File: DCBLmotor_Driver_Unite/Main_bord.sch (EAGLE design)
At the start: 72 parts, among them CN1 DF11-16DP-2DSA, CN2 DF11-16DP-2DSA, CN3 DF11-4DP-2DSR, CN4 HIF3FC-10PA-2.54DSA(71), CN5 HIF3FC-10PA-2.54DSA(71), CN6 0430450612, CN7 0430450612, CN8 BM11B-SRSS-TB, IC1 TMPM370FYFG, IC2 MCP2561FD-E/MF, IC3 AM26C32CD, IC4 AM26C32CD, IC5 LTC2862A, SW1 CVS-02TB, SW2 EVQ-PE104K

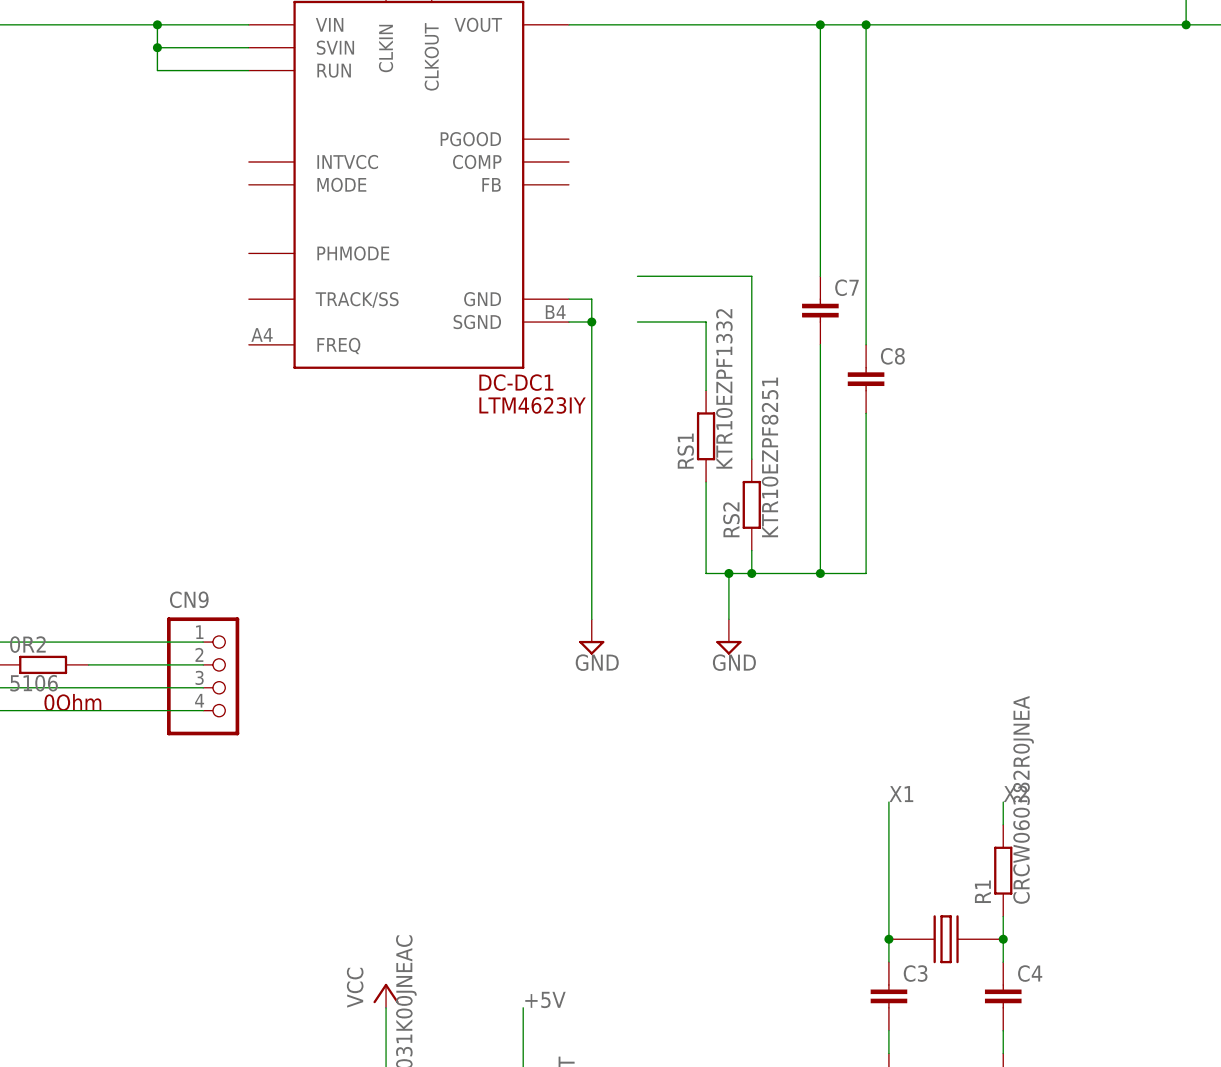
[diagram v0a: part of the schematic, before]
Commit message: Repless to LTM4623
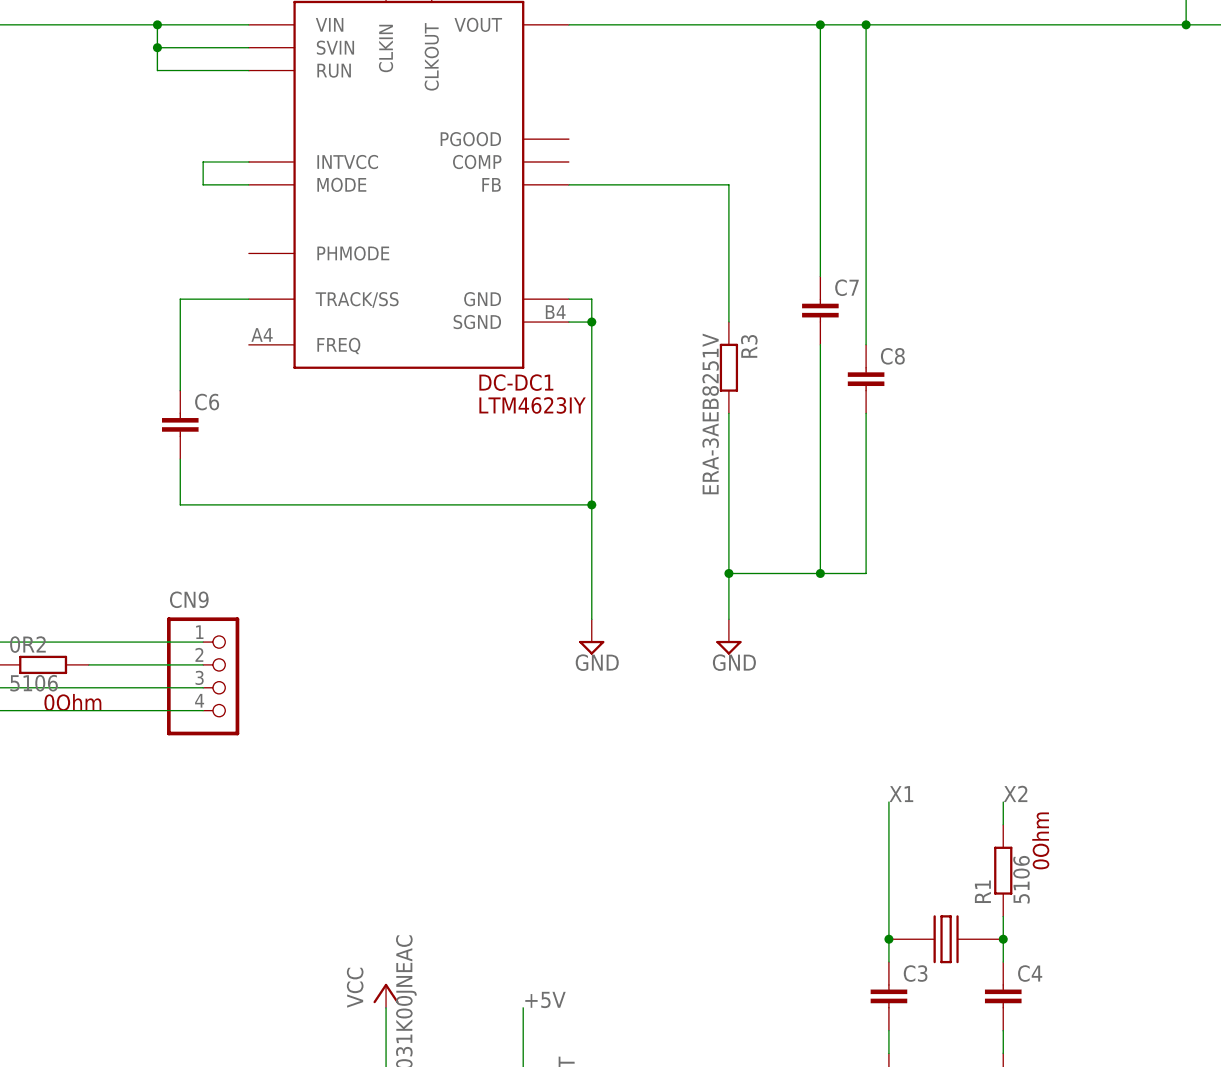
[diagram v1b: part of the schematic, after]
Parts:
- removed RS1: KTR10EZPF1332, ROHM:KTR10EZPF1332
- removed RS2: KTR10EZPF8251, ROHM:KTR10EZPF8251
- added C6: CGA3E2X7R1H104K080AA, TDK:CGA3E2X7R1H104K080AA
- added R3: ERA-3AEB8251V, Panasonic:ERA-3AEB8251V
- R1: value CRCW060382R0JNEA -> 5106; device VISHAY:CRCW060382R0JNEA -> Keystone:5106
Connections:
- removed net N$10: RS2.1
- new net N$12: C6.1, DC-DC1.TRACK/SS
- new net N$45: DC-DC1.INTVCC, DC-DC1.MODE
- net GND: now also C6.2, R3.1; no longer RS1.2, RS2.2
- net N$7: now also DC-DC1.FB, R3.2; no longer RS1.1
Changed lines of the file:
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@@
 <part name="SUPPLY3" library="supply2" library_urn="urn:adsk.eagle:library:372" deviceset="GND" device=""/>
 <part name="SUPPLY5" library="supply2" library_urn="urn:adsk.eagle:library:372" deviceset="GND" device=""/>
-<part name="RS1" library="ROHM" deviceset="KTR10EZPF1332" device=""/>
-<part name="RS2" library="ROHM" deviceset="KTR10EZPF8251" device=""/>
 <part name="SUPPLY8" library="supply2" library_urn="urn:adsk.eagle:library:372" deviceset="GND" device=""/>
 <part name="C7" library="TDK" deviceset="C2012JB0J476M125AC" device=""/>
@@
 <part name="CN1" library="Hirose" deviceset="DF11-16DP-2DSA" device=""/>
 <part name="CN2" library="Hirose" deviceset="DF11-16DP-2DSA" device=""/>
-<part name="R1" library="VISHAY" deviceset="CRCW060382R0JNEA" device=""/>
+<part name="R1" library="Keystone" deviceset="5106" device=""/>
 <part name="L1" library="LQW21HN1R0J00L" deviceset="LQW21HN1R0J00L" device=""/>
 <part name="SUPPLY13" library="supply2" library_urn="urn:adsk.eagle:library:372" deviceset="GND" device=""/>
@@
 <part name="C5" library="KEMET" deviceset="T356L107K016AT" device=""/>
 <part name="DC-DC1" library="LT" deviceset="LTM4623IY" device=""/>
+<part name="C6" library="TDK" deviceset="CGA3E2X7R1H104K080AA" device=""/>
+<part name="R3" library="Panasonic" deviceset="ERA-3AEB8251V" device=""/>
 </parts>
 <sheets>
@@
 <instance part="SUPPLY3" gate="GND" x="416.56" y="-17.78"/>
 <instance part="SUPPLY5" gate="GND" x="78.74" y="-127"/>
-<instance part="RS1" gate="G$1" x="429.26" y="5.08" rot="R90"/>
-<instance part="RS2" gate="G$1" x="434.34" y="-2.54" rot="R90"/>
 <instance part="SUPPLY8" gate="GND" x="431.8" y="-17.78"/>
 <instance part="C7" gate="G$1" x="441.96" y="20.32"/>
@@
 <instance part="C5" gate="G$1" x="439.42" y="220.98"/>
 <instance part="DC-DC1" gate="G$1" x="396.24" y="33.02"/>
+<instance part="C6" gate="G$1" x="370.84" y="7.62"/>
+<instance part="R3" gate="G$1" x="431.8" y="12.7" rot="R270"/>
 </instances>
 <busses>
@@
 <net name="GND" class="0">
 <segment>
-<pinref part="RS1" gate="G$1" pin="2"/>
-<wire x1="429.26" y1="0" x2="429.26" y2="-10.16" width="0.1524" layer="91"/>
-<pinref part="RS2" gate="G$1" pin="2"/>
-<wire x1="434.34" y1="-7.62" x2="434.34" y2="-10.16" width="0.1524" layer="91"/>
-<wire x1="434.34" y1="-10.16" x2="431.8" y2="-10.16" width="0.1524" layer="91"/>
 <pinref part="SUPPLY8" gate="GND" pin="GND"/>
-<wire x1="431.8" y1="-10.16" x2="429.26" y2="-10.16" width="0.1524" layer="91"/>
 <wire x1="431.8" y1="-10.16" x2="431.8" y2="-15.24" width="0.1524" layer="91"/>
-<junction x="431.8" y="-10.16"/>
 <pinref part="C8" gate="G$1" pin="2"/>
-<wire x1="434.34" y1="-10.16" x2="441.96" y2="-10.16" width="0.1524" layer="91"/>
+<wire x1="431.8" y1="-10.16" x2="441.96" y2="-10.16" width="0.1524" layer="91"/>
 <wire x1="441.96" y1="-10.16" x2="447.04" y2="-10.16" width="0.1524" layer="91"/>
 <wire x1="447.04" y1="-10.16" x2="447.04" y2="7.62" width="0.1524" layer="91"/>
-<junction x="434.34" y="-10.16"/>
 <pinref part="C7" gate="G$1" pin="2"/>
 <wire x1="441.96" y1="15.24" x2="441.96" y2="-10.16" width="0.1524" layer="91"/>
 <junction x="441.96" y="-10.16"/>
+<pinref part="R3" gate="G$1" pin="1"/>
+<wire x1="431.8" y1="7.62" x2="431.8" y2="-10.16" width="0.1524" layer="91"/>
+<junction x="431.8" y="-10.16"/>
 </segment>
 <segment>
@@
 <junction x="416.56" y="17.78"/>
 <pinref part="SUPPLY3" gate="GND" pin="GND"/>
-<wire x1="416.56" y1="-15.24" x2="416.56" y2="17.78" width="0.1524" layer="91"/>
-</segment>
-</net>
-<net name="N$7" class="0">
-<segment>
-<pinref part="RS1" gate="G$1" pin="1"/>
-<wire x1="421.64" y1="17.78" x2="429.26" y2="17.78" width="0.1524" layer="91"/>
-<wire x1="429.26" y1="17.78" x2="429.26" y2="10.16" width="0.1524" layer="91"/>
-</segment>
-</net>
-<net name="N$10" class="0">
-<segment>
-<pinref part="RS2" gate="G$1" pin="1"/>
-<wire x1="421.64" y1="22.86" x2="434.34" y2="22.86" width="0.1524" layer="91"/>
-<wire x1="434.34" y1="22.86" x2="434.34" y2="2.54" width="0.1524" layer="91"/>
+<wire x1="416.56" y1="-15.24" x2="416.56" y2="-2.54" width="0.1524" layer="91"/>
+<pinref part="C6" gate="G$1" pin="2"/>
+<wire x1="416.56" y1="-2.54" x2="416.56" y2="17.78" width="0.1524" layer="91"/>
+<wire x1="370.84" y1="2.54" x2="370.84" y2="-2.54" width="0.1524" layer="91"/>
+<wire x1="370.84" y1="-2.54" x2="416.56" y2="-2.54" width="0.1524" layer="91"/>
+<junction x="416.56" y="-2.54"/>
 </segment>
 </net>
@@
 </segment>
 </net>
+<net name="N$12" class="0">
+<segment>
+<pinref part="C6" gate="G$1" pin="1"/>
+<pinref part="DC-DC1" gate="G$1" pin="TRACK/SS"/>
+<wire x1="370.84" y1="10.16" x2="370.84" y2="20.32" width="0.1524" layer="91"/>
+<wire x1="370.84" y1="20.32" x2="378.46" y2="20.32" width="0.1524" layer="91"/>
+</segment>
+</net>
+<net name="N$45" class="0">
+<segment>
+<pinref part="DC-DC1" gate="G$1" pin="INTVCC"/>
+<wire x1="378.46" y1="35.56" x2="373.38" y2="35.56" width="0.1524" layer="91"/>
+<wire x1="373.38" y1="35.56" x2="373.38" y2="33.02" width="0.1524" layer="91"/>
+<pinref part="DC-DC1" gate="G$1" pin="MODE"/>
+<wire x1="373.38" y1="33.02" x2="378.46" y2="33.02" width="0.1524" layer="91"/>
+</segment>
+</net>
+<net name="N$7" class="0">
+<segment>
+<pinref part="DC-DC1" gate="G$1" pin="FB"/>
+<pinref part="R3" gate="G$1" pin="2"/>
+<wire x1="414.02" y1="33.02" x2="431.8" y2="33.02" width="0.1524" layer="91"/>
+<wire x1="431.8" y1="33.02" x2="431.8" y2="17.78" width="0.1524" layer="91"/>
+</segment>
+</net>

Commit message: TEMP Chenge MCU
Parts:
- removed C7, C8: C2012JB0J476M125AC, TDK:C2012JB0J476M125AC
- removed CN10: (no value), jst-xh:B2B-XH-A
- removed CN2: DF11-16DP-2DSA, Hirose:DF11-16DP-2DSA
- removed CN3: DF11-4DP-2DSR, Hirose:DF11-4DP-2DSR
- removed CN4, CN5: HIF3FC-10PA-2.54DSA(71), Hirose:HIF3FC-10PA-2.54DSA(71)
- removed CN6, CN7: 0430450612, Molex:0430450612
- removed CR10, CR11, CR8: NSI50010YT1G, ON Semiconductor:NSI50010YT1G
- removed DC-DC1: LTM4623IY, LT:LTM4623IY
- removed DC10, DC11, DC12, DC13, DC14: YFF21PC1E104MT000N, TDK:YFF21PC1E104MT000N
- removed IC3, IC4: AM26C32CD, AM26C32CD:AM26C32CD
- removed LED2: CL-340T-SD-T, Citizen:CL-340T-SD-T
- removed R1: 5106, Keystone:5106
- removed R3: ERA-3AEB8251V, Panasonic:ERA-3AEB8251V
- removed R4, R5: CRCW060360R4FKEA, VISHAY:CRCW060360R4FKEA
- removed VR1: 3314J-1-104E, Bourns:3314J-1-104E
- C3, C4: value CGA1A2C0G1E180J030BA -> GRM0225C1E120JA03L; device TDK:CGA1A2C0G1E180J030BA -> murata:GRM0225C1E120JA03L
- C5: value T356L107K016AT -> GRM035R60J475ME15D; device KEMET:T356L107K016AT -> murata:GRM035R60J475ME15D
- C6: value CGA3E2X7R1H104K080AA -> GRM035R60J475ME15D; device TDK:CGA3E2X7R1H104K080AA -> murata:GRM035R60J475ME15D
- CN1: value DF11-16DP-2DSA -> FX23L-20S-0.5SV; device Hirose:DF11-16DP-2DSA -> FX23L-20S-0.5SV:FX23L-20S-0.5SV
- DC9: value YFF21PC1E104MT000N -> YFF15PC1C104MT000N; device TDK:YFF21PC1E104MT000N -> TDK:YFF15PC1C104MT000N
- IC2: value MCP2561FD-E/MF -> TMPM373FWDUG; device MicroChip:MCP2561FD-E/MF -> TMPM373FWDUG:TMPM373FWDUG
- XTAL1: value HCM4910000000ABJT -> ABM8AIG-10.000MHZ-12-2Z-T3; device Citizen:HCM4910000000ABJT -> Abracon:ABM8AIG-10.000MHZ-12-2Z-T3
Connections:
- removed net 1SD: CN1.2
- removed net 1_A1: CN4.5, IC3.1B
- removed net 1_A2: CN4.6, IC3.1A
- removed net 1_B1: CN4.7, IC3.2A
- removed net 1_B2: CN4.8, IC3.2B
- removed net 1_I1: CN4.9, IC3.3A
- removed net 1_I2: CN4.10, IC3.3B
- removed net 2SD: CN2.2
- removed net 2_A1: CN5.5, IC4.1B
- removed net 2_A2: CN5.6, IC4.1A
- removed net 2_B1: CN5.7, IC4.2A
- removed net 2_B2: CN5.8, IC4.2B
- removed net CANH: CN3.1, IC2.CANH, R4.1
- removed net CANL: CN3.3, IC2.CANL, R5.1
- removed net N$12: C6.1, DC-DC1.TRACK/SS
- removed net N$28: DC10.P$2, IC4.VCC
- removed net N$29: DC9.P$2, IC3.VCC
- removed net N$30: CN5.2, DC12.P$2
- removed net N$31: CN4.2, DC11.P$2
- removed net N$32: CN6.P$5, DC13.P$2
- removed net N$33: CN7.P$5, DC14.P$2
- removed net N$35: CN5.9, IC4.3A
- removed net N$36: CN5.10, IC4.3B
- removed net N$40: CR8.P$A, LED2.B_C
- removed net N$41: CR11.P$A, LED2.R_C
- removed net N$42: CR10.P$A, LED2.G_C
- removed net N$45: DC-DC1.INTVCC, DC-DC1.MODE
- removed net SPLT: CN3.2, IC2.SPLT, R4.2, R5.2
- removed net VDD: C5.+, CN10.1, DC-DC1.RUN, DC-DC1.SVIN, DC-DC1.VIN
- new net N$10: DC8.P$1, IC2.DVDD5(2)
- net +5V: no longer C7.1, C8.1, DC-DC1.VOUT, DC10.P$1, DC11.P$1, DC12.P$1, DC13.P$1, DC14.P$1, DC8.P$2, DC9.P$1, LED2.A_G, LED2.B_A, LED2.R_A
- net 1U_H: no longer CN1.7
- net 1U_L: no longer CN1.8
- net 1V_H: no longer CN1.3
- net 1V_L: no longer CN1.4
- net 1W_H: no longer CN1.5
- net 1W_L: no longer CN1.6
- net 2U_H: no longer CN2.7
- net 2U_L: no longer CN2.8
- net 2V_H: no longer CN2.3
- net 2V_L: no longer CN2.4
- net 2W_H: no longer CN2.5
- net 2W_L: no longer CN2.6
- net AVDD: no longer VR1.1
- net CU1_1: no longer CN1.15
- net CU1_2: no longer CN1.14
- net CU1_3: no longer CN1.13
- net CU2_1: no longer CN2.15
- net CU2_2: no longer CN2.14
- net CU2_3: no longer CN2.13
- net CVR2: no longer VR1.IO3
- net ENC_A-1: no longer CN6.P$1, IC3.1Y
- net ENC_A-2: no longer CN7.P$1, IC4.1Y
- net ENC_B-1: no longer CN6.P$2, IC3.2Y
- net ENC_B-2: no longer CN7.P$2, IC4.2Y
- net ENC_Z-1: no longer CN6.P$3, IC3.3Y
- net ENC_Z-2: no longer CN7.P$3, IC4.3Y
- net GND: no longer C5.2, C6.2, C7.2, C8.2, CN10.2, CN4.3, CN5.3, CN6.P$4, CN7.P$4, DC-DC1.GND, DC-DC1.SGND, DC10.GND, DC11.GND, DC12.GND, DC13.GND, DC14.GND, DC8.GND, DC9.GND, IC2.VSS, IC3.GND, IC4.GND, R3.1, VR1.2
- net LED2_1: no longer CR10.P$C
- net LED2_2: no longer CR11.P$C
- net LED2_3: no longer CR8.P$C
- net N$11: now also DC9.P$2, IC2.DVDD5(1); no longer C4.1, R1.2, XTAL1.P$2
- net N$6: now also C5.1, IC2.VOUT15; no longer DC8.P$1, IC2.VDD
- net N$7: now also C6.1, IC2.VOUT3; no longer DC-DC1.FB, R3.2
- net RX0: no longer IC2.RXD
- net STBY: no longer IC2.STBY
- net TX0: no longer IC2.TXD
- net X1: now also C4.1, IC2.PM0/X1; no longer C3.1
- net X2: now also C3.1, IC2.PM1/X2, XTAL1.P$2; no longer R1.1
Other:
- moved on the sheet: C3, C4, C6, DC8, DC9

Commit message: Main_borad is Almost_finshed
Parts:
- removed 0R1, 0R2: 5106, Keystone:5106
- removed C1, C2: C2012X7R1A475M125AC, TDK:C2012X7R1A475M125AC
- removed CN8: BM11B-SRSS-TB, JST:BM11B-SRSS-TB
- removed CR1, CR2, CR3, CR4, CR9: C0816X7R1, TDK:C0816X7R1
- removed CR12, CR6, CR7: NSI50010YT1G, ON Semiconductor:NSI50010YT1G
- removed DC3, DC4, DC5: YFF21PC1E104MT000N, TDK:YFF21PC1E104MT000N
- removed DC6, DC7: YFF15PC1C104MT000N, TDK:YFF15PC1C104MT000N
- removed R6, R7: CRCW06031K00JNEAC, VISHAY:CRCW06031K00JNEAC
- removed RA1: EXB-38V103JV, Pana_Chip_RA:EXB-38V103JV
- removed S2: 220AMA16R, 220AMA16R:220AMA16R
- removed VR2: 3314J-1-104E, Bourns:3314J-1-104E
- added CN2: FTSH-105-01-F-DV-K, FTSH-105-01-F-DV-K:FTSH-105-01-F-DV-K
- added R1, R3, R4: MCR006, ROHM:MCR006
- added R5: CRCW06031K00JNEAC, VISHAY:CRCW06031K00JNEAC
- CN9: value (none) -> DF11-4DP-2DSR; device jst-xh:B4B-XH-A -> Hirose:DF11-4DP-2DSR
- DC1, DC2: value YFF21PC1E104MT000N -> YFF15PC1C104MT000N; device TDK:YFF21PC1E104MT000N -> TDK:YFF15PC1C104MT000N
- IC1: value TMPM370FYFG -> ADP3338AKCZ-3.3RL7; device TOSHIBA:TMPM370FYFG -> ADP3338AKCZ-3.3RL7:ADP3338AKCZ-3.3RL7
- SW1: value CVS-02TB -> CVS-01TB; device Nidec:CVS-02TB -> Nidec:CVS-01TB
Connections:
- removed net 1U_H: IC1.UO0/PC0
- removed net 1U_L: IC1.XO0/PC1
- removed net 1V_H: IC1.VO0/PC2
- removed net 1V_L: IC1.YO0/PC3
- removed net 1W_H: IC1.WO0/PC4
- removed net 1W_L: IC1.ZO0/PC5
- removed net 2U_H: IC1.UO1/PG0
- removed net 2U_L: IC1.XO1/PG1
- removed net 2V_H: IC1.VO1/PG2
- removed net 2V_L: IC1.YO1/PG3
- removed net 2W_H: IC1.WO1/PG4
- removed net 2W_L: IC1.ZO1/PG5
- removed net AGND: CR9.2, DC2.GND, IC1.AMPVSS
- removed net CU1_1: IC1.PH0/AINA0/INT0
- removed net CU1_2: IC1.PH1/AINA1/INT1
- removed net CU1_3: IC1.PH2/AINA2/INT2
- removed net CU2_1: IC1.PI1/AINA9/AINB0
- removed net CU2_2: IC1.PI2/AINA10/AINB1
- removed net CU2_3: IC1.PI3/AINA11/AINB2
- removed net CVR1: IC1.CVREFABC, VR2.IO3
- removed net CVR2: IC1.CVREFD
- removed net DIP1: IC1.PJ0/AINB3, RA1-4.2, S2.1
- removed net DIP2: IC1.PJ1/AINB4, RA1-1.2, S2.2
- removed net DIP4: IC1.PJ2/AINB5, RA1-3.2, S2.4
- removed net DIP8: IC1.PJ3/AINB6, RA1-2.2, S2.8
- removed net EMG1: IC1.EMG0/PC6
- removed net EMG2: IC1.EMG1/PG6
- removed net ENC_A-1: IC1.TB5IN/ENCA0/PD0
- removed net ENC_A-2: IC1.PF2/ENCA1/SCLK3/CTS3
- removed net ENC_B-1: IC1.TB5OUT/ENCB0/PD1
- removed net ENC_B-2: IC1.PF3/ENCB1/TXD3
- removed net ENC_Z-1: IC1.ENCZ0/PD2
- removed net ENC_Z-2: IC1.PF4/ENCZ1/RXD3
- removed net LED1_1: CR6.P$C, IC1.CTS0/SCLK0/PE2
- removed net LED1_2: CR12.P$C, IC1.TB4OUT/PE3
- removed net LED1_3: CR7.P$C, IC1.INT5/TB2IN/PE4
- removed net LED2_1: IC1.TB2OUT/PE5
- removed net LED2_2: IC1.INT6/TB3IN/PE6
- removed net LED2_3: IC1.INT7/TB3OUT/PE7
- removed net N$13: IC1.RXD2/PD6
- removed net N$14: DC6.P$1, IC1.AVDD5A/VREFHA
- removed net N$15: DC7.P$1, IC1.AVDD5B/VREFHB
- removed net N$16: IC1.DVSS0
- removed net N$17: IC1.TXD2/PD5
- removed net N$18: CN8.P$5, IC1.PB4/TCK/SWCLK
- removed net N$19: CN8.P$6, IC1.PB3/TMS/SWDIO
- removed net N$20: CN8.P$9, IC1.PB0/TRACECLK
- removed net N$21: CN8.P$7, IC1.PB2/TRACEDATA-1
- removed net N$22: CN8.P$8, IC1.PB1/TRACEDATA-0
- removed net N$23: CN8.P$4, IC1.PB5/TDO/SWV
- removed net N$24: CN8.P$3, IC1.PB6/TDI
- removed net N$25: CN8.P$2, IC1.PB7/TRST
- removed net N$26: IC1.CTS2/SCLK2/PD4
- removed net N$27: IC1.INT9/PD3
- removed net N$37: CR7.P$A, LED1.B_C
- removed net N$38: CR12.P$A, LED1.R_C
- removed net N$39: CR6.P$A, LED1.G_C
- removed net N$44: 0R2.1, CN9.2
- removed net N$46: 0R1.1, CN9.1
- removed net N$8: C1.1, IC1.VOUT15
- removed net N$9: C2.1, IC1.VOUT3
- removed net RX0: IC1.RXD0/PE1, IC5.DI
- removed net STBY: IC1.INT8/TB4IN/PA7
- removed net SW1: IC1.PJ4/AINB7, R6.2, SW1G$1.P
- removed net SW2: IC1.PJ5/AINB8, R7.2, SW1G$2.P
- removed net TX0: IC1.TXD0/PE0, IC5.RO
- new net +3.3V: IC1.OUT, IC1.OUT_1
- new net BOOT: IC2.PF0/TB7IN/BOOT, R5.2, SW1.S
- new net CU1: CN1G$1.1, IC2.PJ5/AINB8
- new net HIN1: CN1G$1.19, IC2.PG0/UO1
- new net HIN2: CN1G$1.16, IC2.PG2/VO1
- new net HIN3: CN1G$1.18, IC2.PG4/WO1
- new net LED_1: IC2.PE0/TXD0, R4.2
- new net LED_2: IC2.PE1/RXD0, R3.2
- new net LED_3: IC2.PE2/SCLK0/CTS0, R1.2
- new net LIN1: CN1G$1.15, IC2.PG1/XO1
- new net LIN2: CN1G$1.20, IC2.PG3/YO1
- new net LIN3: CN1G$1.17, IC2.PG5/ZO1
- new net N$31: CN2.7
- new net N$32: CN2.9
- new net RXD1: IC2.PA6/TB6IN/RXD1, IC5.DI
- new net TCK: CN2.4, IC2.PB4/TCK/SWCLK
- new net TDI: CN2.8, IC2.PB6/TDI
- new net TDO: CN2.6, IC2.PB5/TDO/SWV
- new net TMS: CN2.2, IC2.PB3/TMS/SWDIO
- new net TXD1: IC2.PA5/TB6OUT/TXD1, IC5.RO
- net +5V: now also CN1G$2.3, CN2.1, CN9.2, DC8.P$2, DC9.P$1, IC1.IN, R2.1, R5.1; no longer 0R2.2, CN8.P$1, CR1.1, CR2.1, CR3.1, CR4.1, CR9.1, DC1.P$1, DC3.P$2, DC4.P$2, DC5.P$1, R6.1, R7.1, RA1-1.1, RA1-2.1, RA1-3.1, RA1-4.1
- net AVDD: now also DC1.P$2; no longer DC6.P$2, DC7.P$2, VR2.1
- net GND: now also C5.2, C6.2, CN1G$2.2, CN2.3, CN2.5, CN9.1, DC2.GND, DC8.GND, DC9.GND, IC1.GND, IC2.AVSSB/VREFB, IC2.DVSS(1), IC2.DVSS(2), IC2.MODE, SW1.P; no longer 0R1.2, C1.2, C2.2, CR1.2, CR2.2, CR3.2, CR4.2, DC3.GND, DC4.GND, DC5.GND, DC6.GND, DC7.GND, IC1.AVSSA/VREFLA, IC1.AVSSB/VREFLB, IC1.DVSS1, IC1.DVSS2, IC1.DVSS3, IC1.DVSS4, IC1.DVSS5, IC1.MODE, S2.C(1), S2.C(2), SW1G$1.S, SW1G$2.S, VR2.2
- net N$1: now also DC2.P$1, IC2.RVDD5; no longer DC5.P$2, IC1.DVDD5_1
- net N$2: now also DC1.P$1, IC2.AVDD5B/VREFHB; no longer DC4.P$1, IC1.RVDD5
- net N$3: now also LED1.R_C, R3.1; no longer DC3.P$1, IC1.DVDD5E
- net N$4: now also LED1.B_C, R1.1; no longer DC2.P$1, IC1.AMPVDD5
- net N$5: now also LED1.G_C, R4.1; no longer DC1.P$2, IC1.DVDD5_0
- net RESET: now also CN2.10, IC2.RESET; no longer CN8.P$10, IC1.RESET
- net RS_DIR: now also IC2.PA4/CTS1/SCLK1; no longer IC1.TB6IN/RXD1/PA6
- net VCC: now also CN1G$2.1; no longer R2.1
- net X1: no longer IC1.X1
- net X2: no longer IC1.X2
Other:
- note removed: "JTAG"
- moved on the sheet: C3, C4, C5, C6, CN1G$1, CN1G$2, CN9, CR5, DC1, DC15, DC2, DC8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

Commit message: Temp Commit
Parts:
- added CN3: DF11-16DP-2DSA, Hirose:DF11-16DP-2DSA
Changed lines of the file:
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@@
 <part name="SUPPLY1" library="supply2" library_urn="urn:adsk.eagle:library:372" deviceset="GND" device=""/>
 <part name="IC1" library="ADP3338AKCZ-3.3RL7" deviceset="ADP3338AKCZ-3.3RL7" device=""/>
+<part name="CN3" library="Hirose" deviceset="DF11-16DP-2DSA" device=""/>
 </parts>
 <sheets>
@@
 <instance part="SUPPLY1" gate="GND" x="187.96" y="60.96"/>
 <instance part="IC1" gate="G$1" x="-76.2" y="60.96"/>
+<instance part="CN3" gate="G$1" x="220.98" y="205.74"/>
 </instances>
 <busses>
